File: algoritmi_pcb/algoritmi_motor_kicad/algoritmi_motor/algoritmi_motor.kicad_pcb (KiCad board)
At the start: 2 copper layers, 32 x 32 mm, 3 parts, among them J1 TSM-105-01-F-SH, U1 MT6701-CT

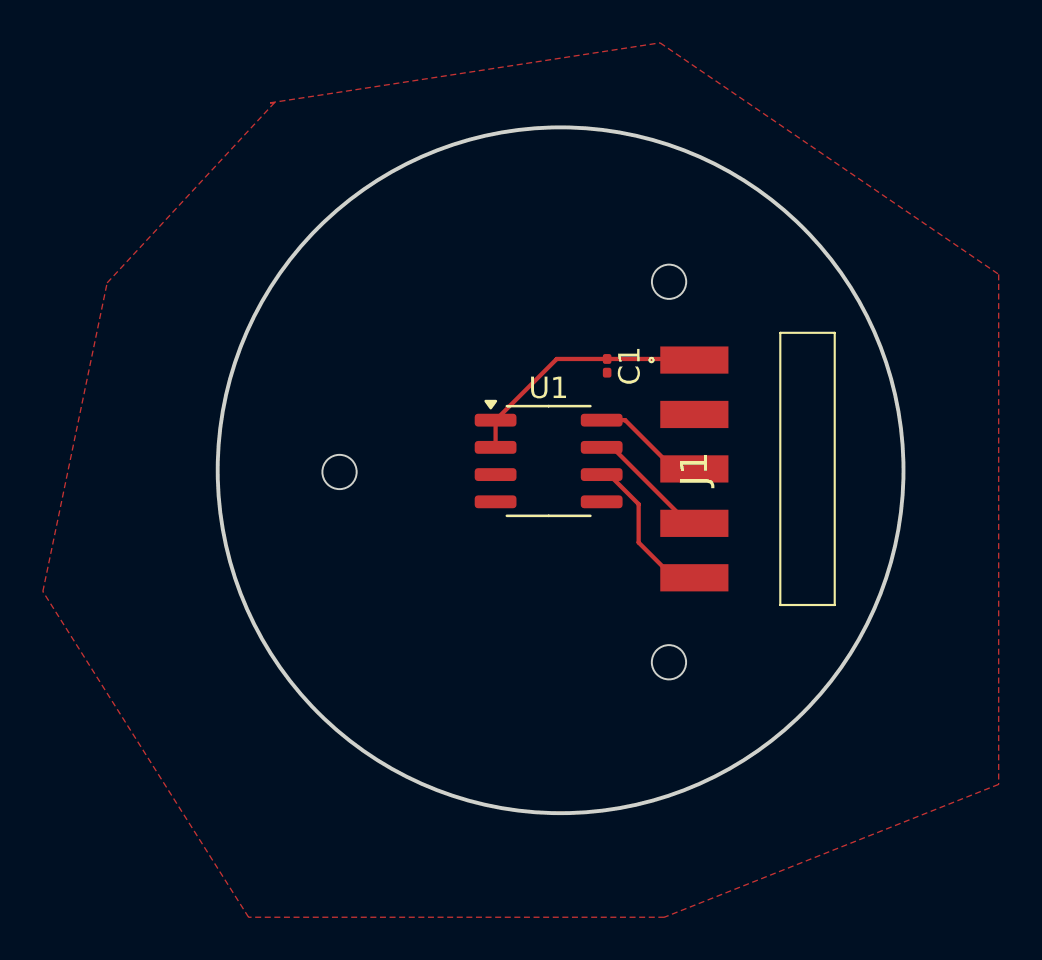
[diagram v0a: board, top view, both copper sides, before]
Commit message: All 3 PCBs done
There's still work left: generate all the BOMs and re-check all the circuits and see if nothing is wrong.
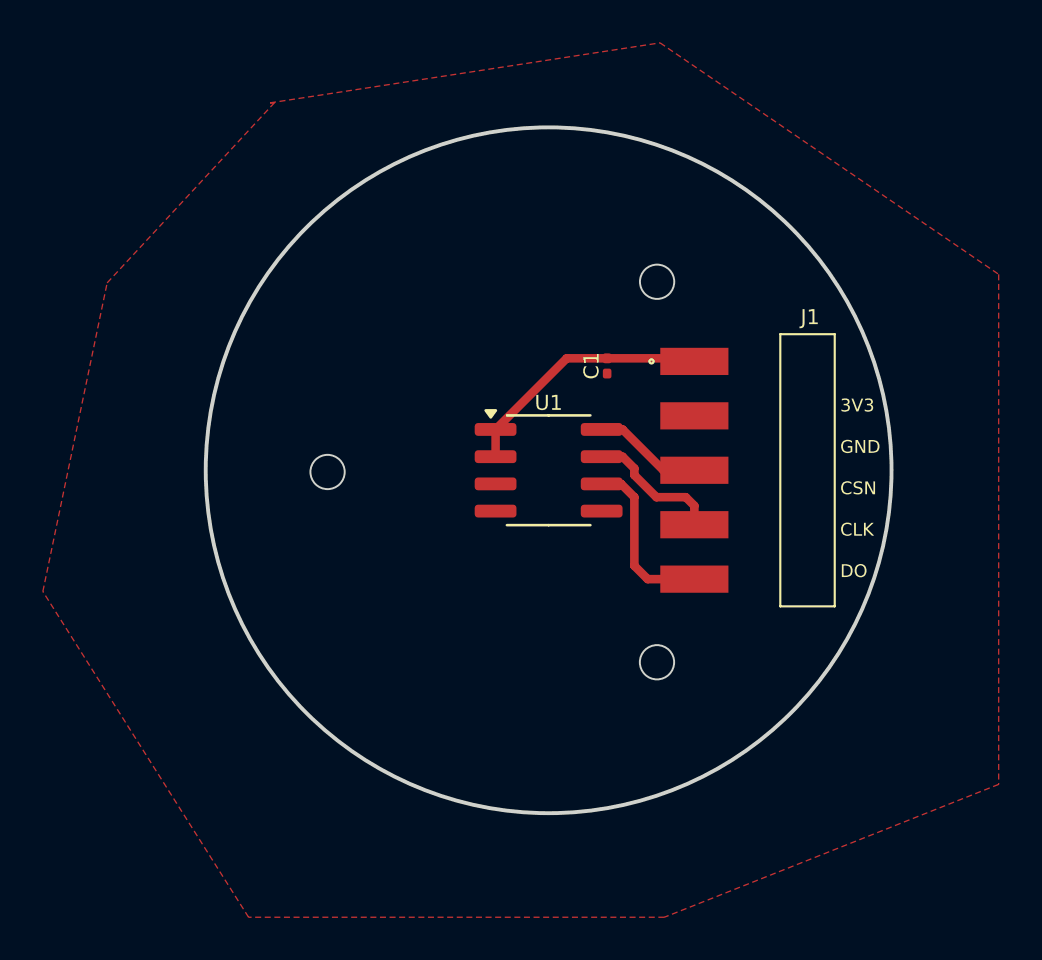
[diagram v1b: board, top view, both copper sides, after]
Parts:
- moved U1 0.43 mm to (141.0, 100.3)
- moved J1 0.06 mm to (147.8, 100.3)
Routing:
- net DO: track 7.37 -> 8.04 mm
- net CLK: track 5.79 -> 6.34 mm
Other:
- board text added: "3V3 GND CSN CLK DO"
